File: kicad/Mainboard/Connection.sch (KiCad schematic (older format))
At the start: 12 parts, among them J13 GPS_CONN, J14 Micro_SD_Card, J15 DBG_CONN, U11 LSM9DS1

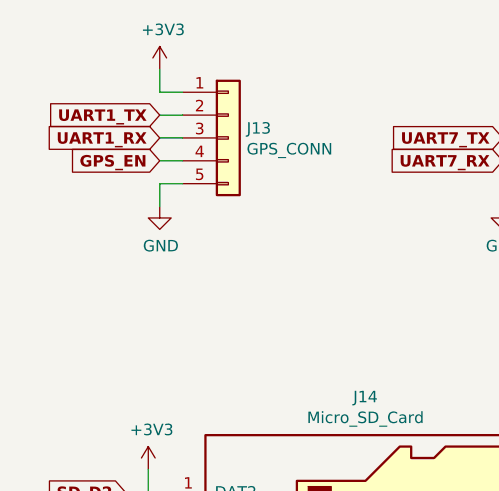
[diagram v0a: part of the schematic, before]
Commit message: added a capacitor for GPS voltage line footprints - expanded RF transistors ground plane generated new PDF added authors
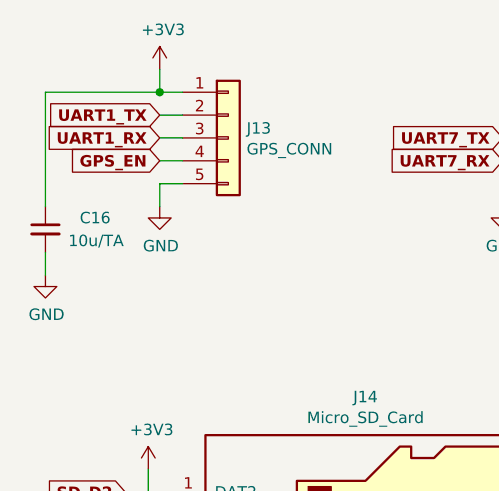
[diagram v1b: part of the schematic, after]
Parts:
- added C16: 10u/TA, Capacitor_Tantalum_SMD:CP_EIA-3216-18_Kemet-A, symbol Mainboard-rescue:C_Small-device
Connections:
- net +3V3: now also C16.1
- net GND: now also C16.2
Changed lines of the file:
@@
 Comment1 ""
 Comment2 ""
-Comment3 ""
+Comment3 "Author: DB9MAT Mathis, SO3ALG Nikoloz, SP5WWP Wojciech"
 Comment4 "TR-9 Open Source Digital Radio"
 $EndDescr
@@
 P 3000 1750
 AR Path="/5DEDCA32/5E4F7B10" Ref="#PWR?"  Part="1"
-AR Path="/5E07B88F/5E4F7B10" Ref="#PWR?"  Part="1"
-F 0 "#PWR?" H 3000 1600 50  0001 C CNN
+AR Path="/5E07B88F/5E4F7B10" Ref="#PWR0155"  Part="1"
+F 0 "#PWR0155" H 3000 1600 50  0001 C CNN
 F 1 "+3V3" H 3015 1923 50  0000 C CNN
 F 2 "" H 3000 1750 50  0001 C CNN
@@
 	1    0    0    -1
 $EndComp
+$Comp
+L Mainboard-rescue:C_Small-device C?
+U 1 1 5E532555
+P 2500 2450
+AR Path="/5DEDCA32/5E532555" Ref="C?"  Part="1"
+AR Path="/5E07B88F/5E532555" Ref="C16"  Part="1"
+F 0 "C16" H 2650 2500 50  0000 L CNN
+F 1 "10u/TA" H 2600 2400 50  0000 L CNN
+F 2 "Capacitor_Tantalum_SMD:CP_EIA-3216-18_Kemet-A" H 2500 2450 50  0001 C CNN
+F 3 "~" H 2500 2450 50  0001 C CNN
+F 4 "TAJA226K006RNJV" H 2500 2450 50  0001 C CNN "Partno"
+	1    2500 2450
+	1    0    0    -1
+$EndComp
+Wire Wire Line
+	2500 2350 2500 1850
+Wire Wire Line
+	2500 1850 3000 1850
+Connection ~ 3000 1850
+$Comp
+L power:GND #PWR0181
+U 1 1 5E5377E4
+P 2500 2650
+F 0 "#PWR0181" H 2500 2400 50  0001 C CNN
+F 1 "GND" H 2505 2477 50  0000 C CNN
+F 2 "" H 2500 2650 50  0001 C CNN
+F 3 "" H 2500 2650 50  0001 C CNN
+	1    2500 2650
+	1    0    0    -1
+$EndComp
+Wire Wire Line
+	2500 2550 2500 2650
 $EndSCHEMATC

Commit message: PCB - connected microSD card to STM32 & USB frontend path routed added a schottky diode PMEG4005ET.215 footprint changed connector J7 pinout - TFT_RST swapped with UART2_RX! schootky diode added to in series to mini USB connector PDF generated
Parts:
- J15: footprint Connector_PinHeader_2.54mm:PinHeader_1x03_P2.54mm_Vertical -> Connector_PinHeader_1.27mm:PinHeader_1x03_P1.27mm_Vertical
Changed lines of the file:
@@
 F 0 "J15" H 4880 2192 50  0000 L CNN
 F 1 "DBG_CONN" H 4880 2101 50  0000 L CNN
-F 2 "Connector_PinHeader_2.54mm:PinHeader_1x03_P2.54mm_Vertical" H 4800 2150 50  0001 C CNN
+F 2 "Connector_PinHeader_1.27mm:PinHeader_1x03_P1.27mm_Vertical" H 4800 2150 50  0001 C CNN
 F 3 "~" H 4800 2150 50  0001 C CNN
 	1    4800 2150

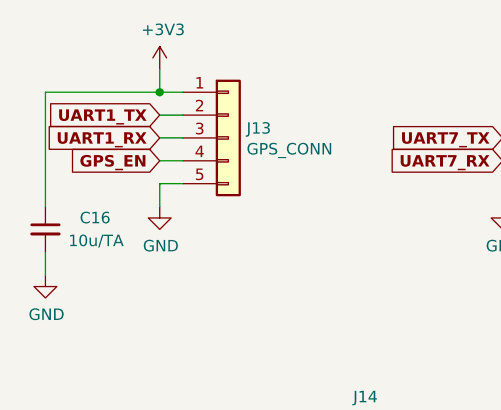
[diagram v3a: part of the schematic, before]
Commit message: RF path improvement, changing speaker and microphone headers to soldering pads, plotting new PDF
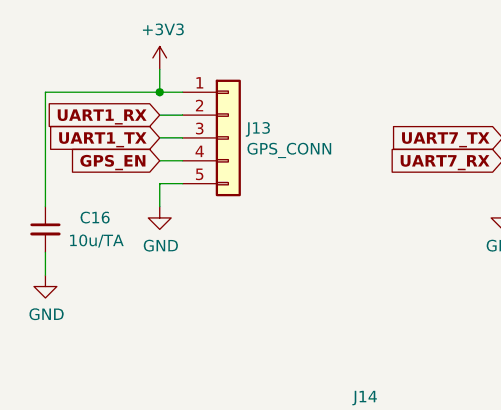
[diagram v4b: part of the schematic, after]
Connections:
- net UART1_RX: now also J13.2 (Pin_2); no longer J13.3 (Pin_3)
- net UART1_TX: now also J13.3 (Pin_3); no longer J13.2 (Pin_2)
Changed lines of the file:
@@
 Wire Wire Line
 	3100 2050 3000 2050
+Text GLabel 3000 2050 0    50   Input ~ 10
+UART1_TX
 Text GLabel 3000 1950 0    50   Input ~ 10
-UART1_TX
-Text GLabel 3000 2050 0    50   Input ~ 10
 UART1_RX
 $Comp

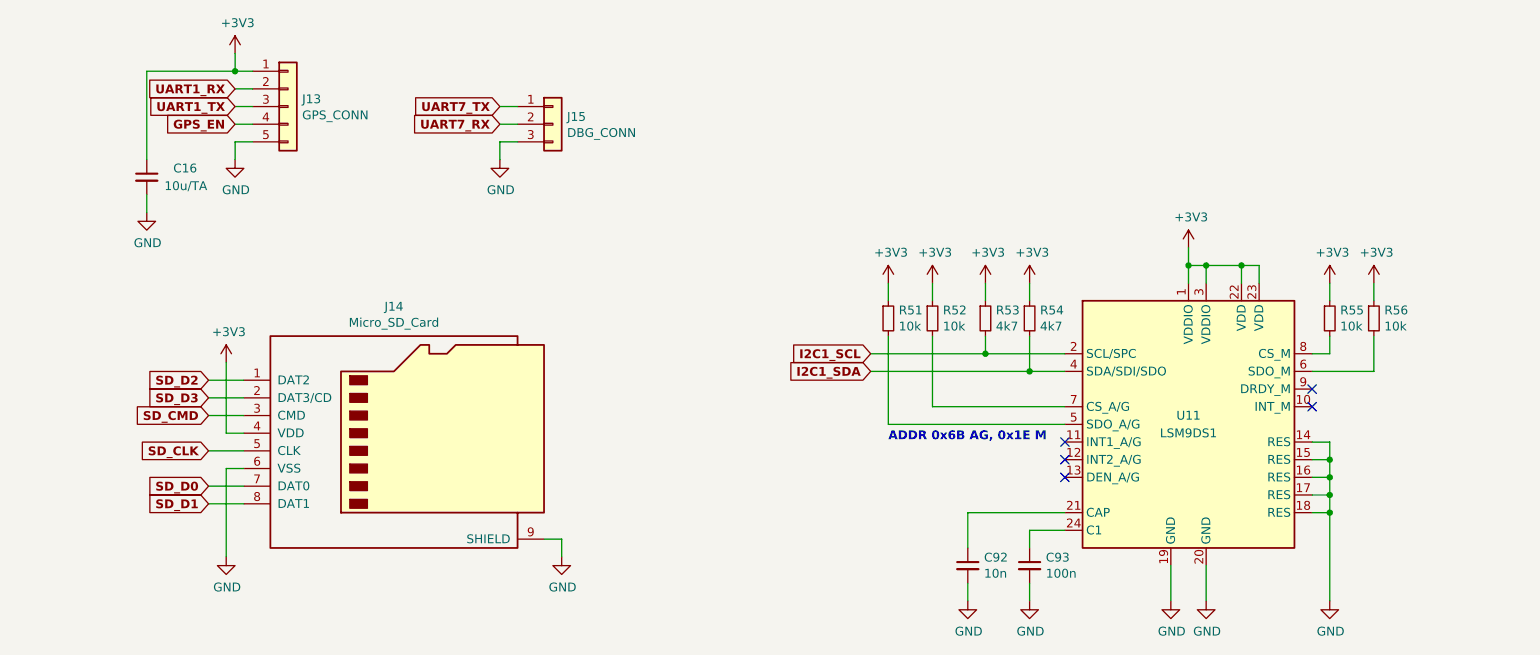
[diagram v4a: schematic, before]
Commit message: added some decoupling caps, pull ups/downs
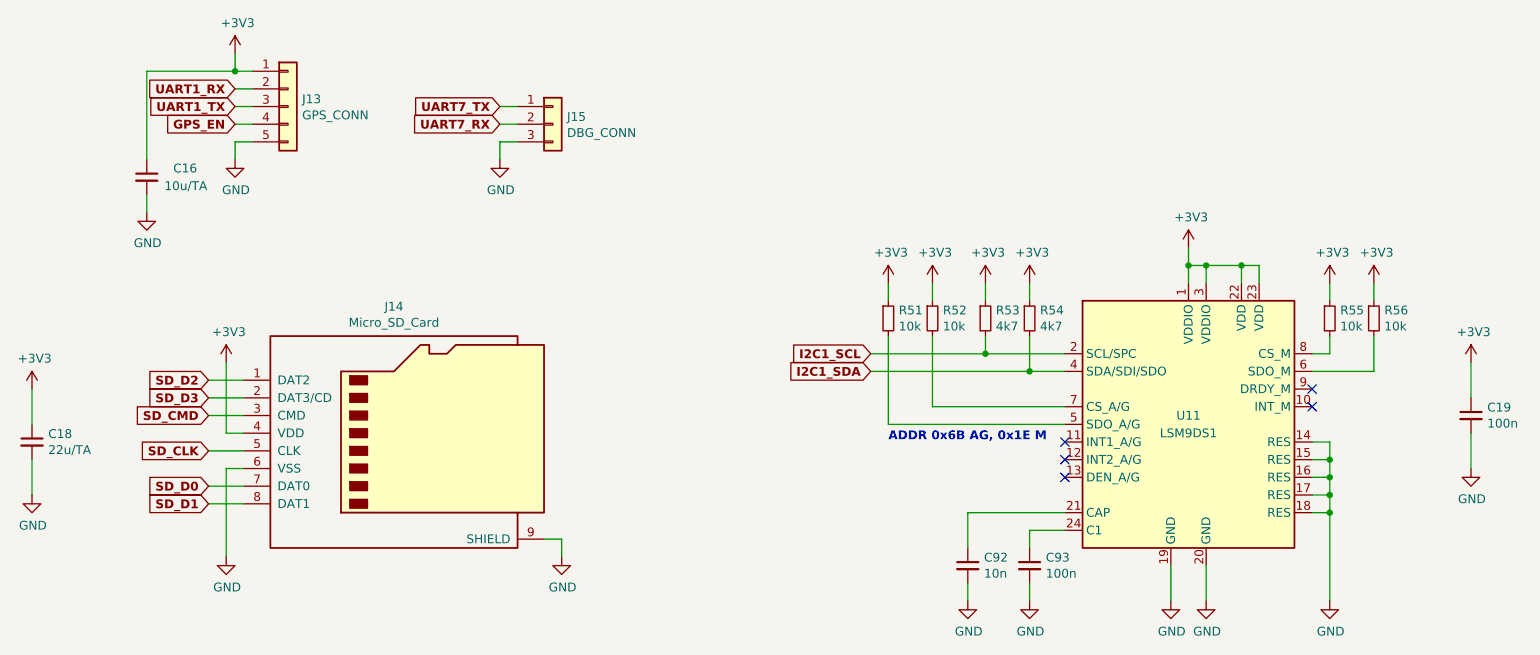
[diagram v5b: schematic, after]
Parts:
- added C18: 22u/TA, Capacitor_Tantalum_SMD:CP_EIA-3216-18_Kemet-A, symbol Mainboard-rescue:C_Small-device
- added C19: 100n, Capacitor_SMD:C_0603_1608Metric, symbol Mainboard-rescue:C_Small-Device
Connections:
- net +3V3: now also C18.1, C19.1
- net GND: now also C18.2, C19.2
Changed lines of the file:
@@
 Wire Wire Line
 	2500 2550 2500 2650
+$Comp
+L Mainboard-rescue:C_Small-device C?
+U 1 1 5E5507D1
+P 1850 3950
+AR Path="/5DEDCA32/5E5507D1" Ref="C?"  Part="1"
+AR Path="/5E07B88F/5E5507D1" Ref="C18"  Part="1"
+F 0 "C18" H 1942 3996 50  0000 L CNN
+F 1 "22u/TA" H 1942 3905 50  0000 L CNN
+F 2 "Capacitor_Tantalum_SMD:CP_EIA-3216-18_Kemet-A" H 1850 3950 50  0001 C CNN
+F 3 "~" H 1850 3950 50  0001 C CNN
+F 4 "TAJA226K006RNJV" H 1850 3950 50  0001 C CNN "Partno"
+	1    1850 3950
+	1    0    0    -1
+$EndComp
+$Comp
+L power:+3V3 #PWR?
+U 1 1 5E5507DB
+P 1850 3650
+AR Path="/5DEDCA32/5E5507DB" Ref="#PWR?"  Part="1"
+AR Path="/5E07B88F/5E5507DB" Ref="#PWR0202"  Part="1"
+F 0 "#PWR0202" H 1850 3500 50  0001 C CNN
+F 1 "+3V3" H 1865 3823 50  0000 C CNN
+F 2 "" H 1850 3650 50  0001 C CNN
+F 3 "" H 1850 3650 50  0001 C CNN
+	1    1850 3650
+	1    0    0    -1
+$EndComp
+$Comp
+L power:GND #PWR?
+U 1 1 5E5507E3
+P 1850 4250
+AR Path="/5DEDCA32/5E5507E3" Ref="#PWR?"  Part="1"
+AR Path="/5E07B88F/5E5507E3" Ref="#PWR0203"  Part="1"
+F 0 "#PWR0203" H 1850 4000 50  0001 C CNN
+F 1 "GND" H 1855 4077 50  0000 C CNN
+F 2 "" H 1850 4250 50  0001 C CNN
+F 3 "" H 1850 4250 50  0001 C CNN
+	1    1850 4250
+	1    0    0    -1
+$EndComp
+Wire Wire Line
+	1850 3650 1850 3850
+Wire Wire Line
+	1850 4050 1850 4250
+$Comp
+L power:+3V3 #PWR?
+U 1 1 5E5F95AC
+P 10000 3500
+AR Path="/5DEDCA32/5E5F95AC" Ref="#PWR?"  Part="1"
+AR Path="/5E07B88F/5E5F95AC" Ref="#PWR0204"  Part="1"
+F 0 "#PWR0204" H 10000 3350 50  0001 C CNN
+F 1 "+3V3" H 10015 3673 50  0000 C CNN
+F 2 "" H 10000 3500 50  0001 C CNN
+F 3 "" H 10000 3500 50  0001 C CNN
+	1    10000 3500
+	1    0    0    -1
+$EndComp
+$Comp
+L power:GND #PWR?
+U 1 1 5E5F95B2
+P 10000 4100
+AR Path="/5DEDCA32/5E5F95B2" Ref="#PWR?"  Part="1"
+AR Path="/5E07B88F/5E5F95B2" Ref="#PWR0205"  Part="1"
+F 0 "#PWR0205" H 10000 3850 50  0001 C CNN
+F 1 "GND" H 10005 3927 50  0000 C CNN
+F 2 "" H 10000 4100 50  0001 C CNN
+F 3 "" H 10000 4100 50  0001 C CNN
+	1    10000 4100
+	1    0    0    -1
+$EndComp
+Wire Wire Line
+	10000 3500 10000 3700
+Wire Wire Line
+	10000 3900 10000 4100
+$Comp
+L Mainboard-rescue:C_Small-Device C19
+U 1 1 5E5FADFD
+P 10000 3800
+F 0 "C19" H 10092 3846 50  0000 L CNN
+F 1 "100n" H 10092 3755 50  0000 L CNN
+F 2 "Capacitor_SMD:C_0603_1608Metric" H 10000 3800 50  0001 C CNN
+F 3 "~" H 10000 3800 50  0001 C CNN
+	1    10000 3800
+	1    0    0    -1
+$EndComp
 $EndSCHEMATC

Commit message: added few values in BOM
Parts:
- C16: value 10u/TA -> 22u/TA; Tolerance (none) -> 10; Voltage (none) -> 6.3
- C18: Tolerance (none) -> 10; Voltage (none) -> 6.3
- C19, C92, C93: Tolerance (none) -> 10; Voltage (none) -> 25
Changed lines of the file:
@@
 F 2 "Capacitor_SMD:C_0603_1608Metric" H 7500 4650 50  0001 C CNN
 F 3 "~" H 7500 4650 50  0001 C CNN
+F 4 "25" H 7500 4650 50  0001 C CNN "Voltage"
+F 5 "10" H 7500 4650 50  0001 C CNN "Tolerance"
 	1    7500 4650
 	1    0    0    -1
@@
 F 2 "Capacitor_SMD:C_0603_1608Metric" H 7150 4650 50  0001 C CNN
 F 3 "~" H 7150 4650 50  0001 C CNN
+F 4 "10" H 7150 4650 50  0001 C CNN "Tolerance"
+F 5 "25" H 7150 4650 50  0001 C CNN "Voltage"
 	1    7150 4650
 	1    0    0    -1
@@
 AR Path="/5E07B88F/5E532555" Ref="C16"  Part="1"
 F 0 "C16" H 2650 2500 50  0000 L CNN
-F 1 "10u/TA" H 2600 2400 50  0000 L CNN
+F 1 "22u/TA" H 2600 2400 50  0000 L CNN
 F 2 "Capacitor_Tantalum_SMD:CP_EIA-3216-18_Kemet-A" H 2500 2450 50  0001 C CNN
 F 3 "~" H 2500 2450 50  0001 C CNN
 F 4 "TAJA226K006RNJV" H 2500 2450 50  0001 C CNN "Partno"
+F 5 "10" H 2500 2450 50  0001 C CNN "Tolerance"
+F 6 "6.3" H 2500 2450 50  0001 C CNN "Voltage"
 	1    2500 2450
 	1    0    0    -1
@@
 F 3 "~" H 1850 3950 50  0001 C CNN
 F 4 "TAJA226K006RNJV" H 1850 3950 50  0001 C CNN "Partno"
+F 5 "10" H 1850 3950 50  0001 C CNN "Tolerance"
+F 6 "6.3" H 1850 3950 50  0001 C CNN "Voltage"
 	1    1850 3950
 	1    0    0    -1
@@
 F 2 "Capacitor_SMD:C_0603_1608Metric" H 10000 3800 50  0001 C CNN
 F 3 "~" H 10000 3800 50  0001 C CNN
+F 4 "25" H 10000 3800 50  0001 C CNN "Voltage"
+F 5 "10" H 10000 3800 50  0001 C CNN "Tolerance"
 	1    10000 3800
 	1    0    0    -1
